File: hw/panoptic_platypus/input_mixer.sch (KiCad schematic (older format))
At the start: 9 parts

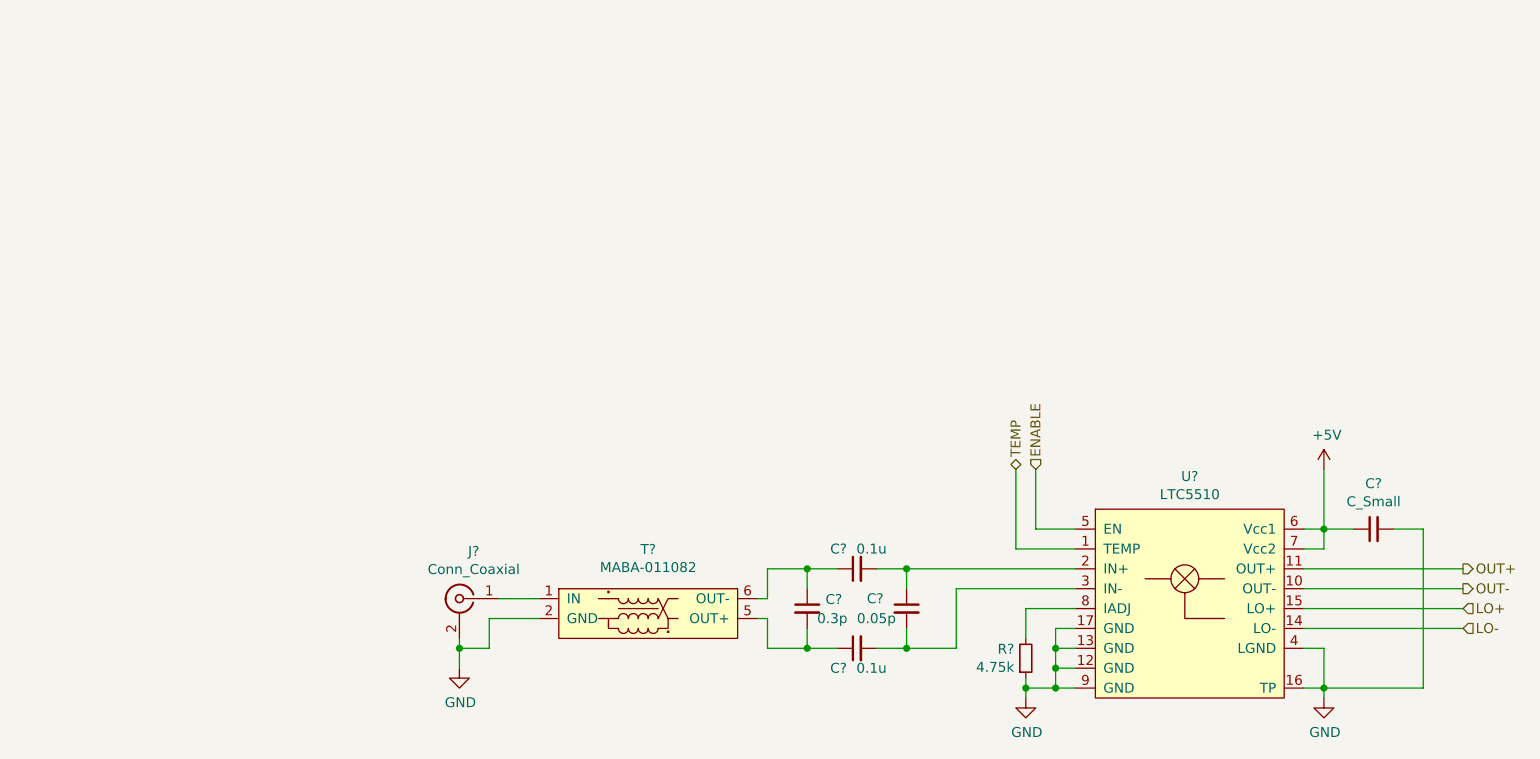
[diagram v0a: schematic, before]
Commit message: Added ADC decoupling and input filter
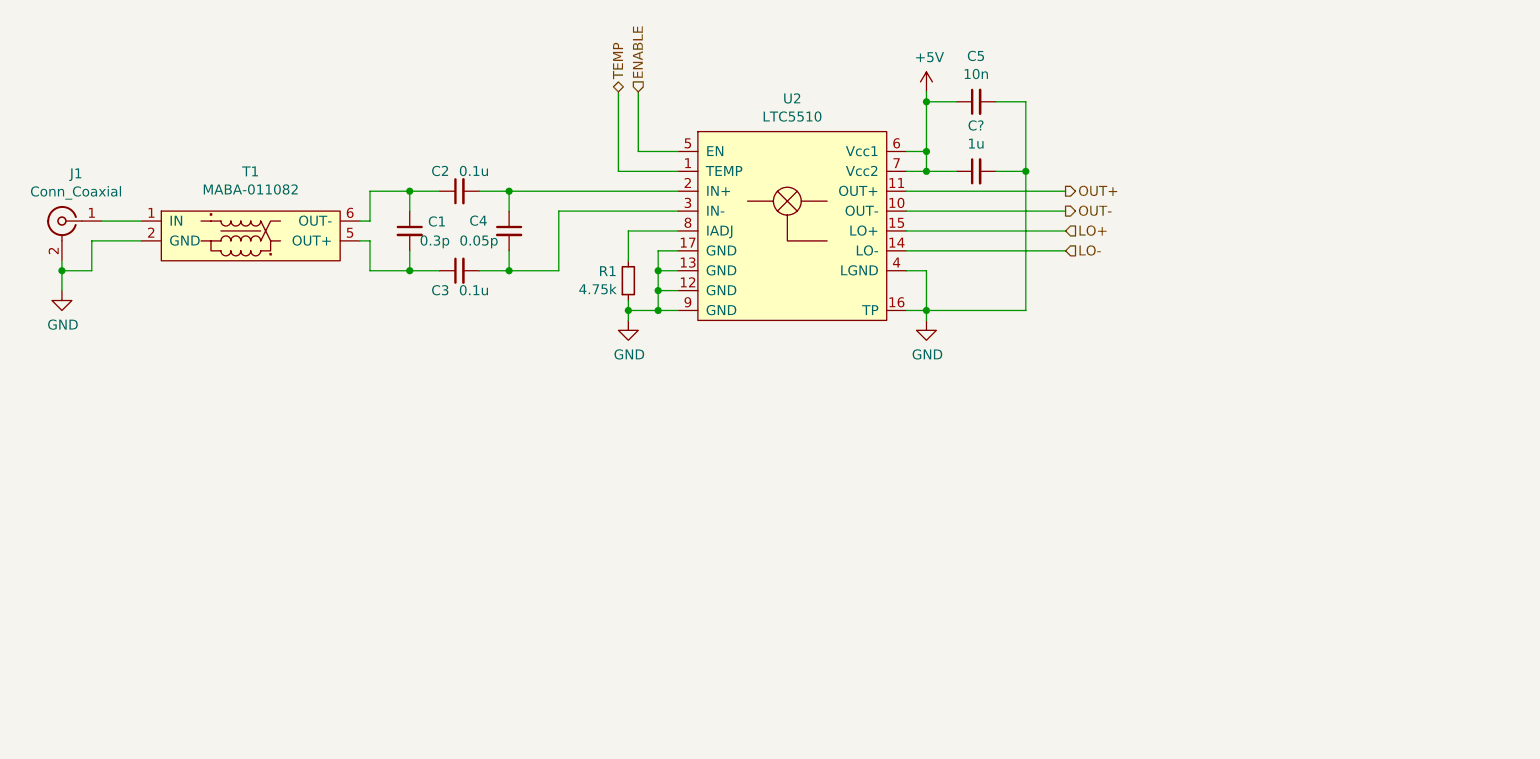
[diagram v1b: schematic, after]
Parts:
- added C?: 1u, symbol Device:C_Small
- C5: renamed from C?; value C_Small -> 10n
- gave numbers to parts that had none: 8
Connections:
- net +5V: now also C?.1
- net GND: now also C?.2
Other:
- moved on the sheet: C1, C2, C3, C4, C5, J1, R1, T1, U2

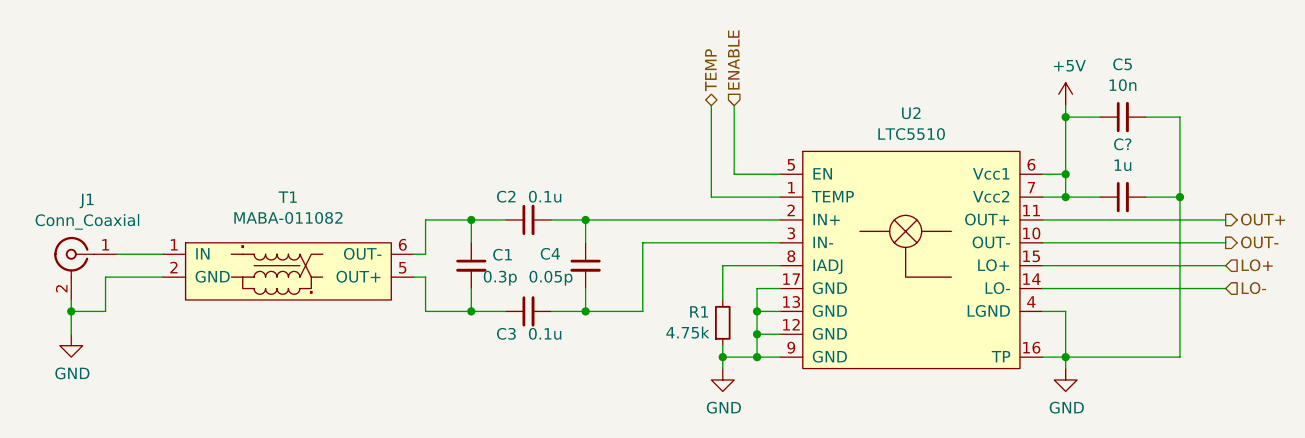
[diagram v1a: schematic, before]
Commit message: updated some symbols added some ICs
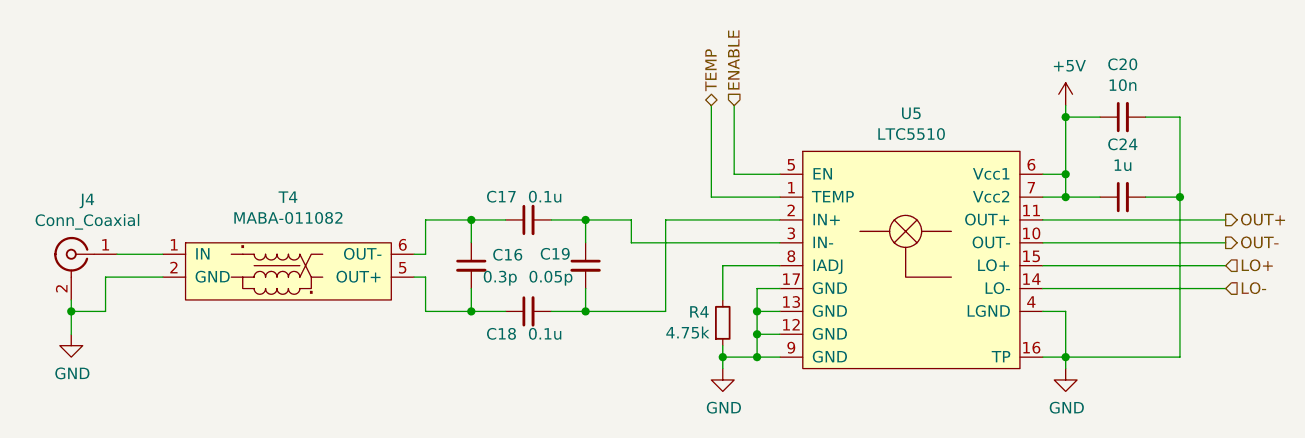
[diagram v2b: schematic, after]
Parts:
- C1, C2, C3, C4, C5: footprint (none) -> Capacitor_SMD:C_0402_1005Metric
- C21: renamed from C?; footprint (none) -> Capacitor_SMD:C_0402_1005Metric
- J1: footprint (none) -> Connector_Coaxial:SMA_Amphenol_132289_EdgeMount
- R1: footprint (none) -> Resistor_SMD:R_0402_1005Metric
- T1: footprint (none) -> Transformer_SMD:Pulse_P0926NL
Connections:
- net at C2.2, C4.1: now also U2.3 (IN-); no longer U2.2 (IN+)
- net at C3.2, C4.2: now also U2.2 (IN+); no longer U2.3 (IN-)
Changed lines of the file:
@@
 $Descr A4 11693 8268
 encoding utf-8
-Sheet 2 6
+Sheet 5 9
 Title ""
 Date "2020-09-21"
@@
 AR Path="/5F682454/5F68ECDE" Ref="J3"  Part="1"
 AR Path="/5F682640/5F68ECDE" Ref="J4"  Part="1"
-F 0 "J1" H 1128 2338 50  0000 C CNN
+F 0 "J4" H 1128 2338 50  0000 C CNN
 F 1 "Conn_Coaxial" H 1128 2247 50  0000 C CNN
-F 2 "" H 1200 2100 50  0001 C CNN
+F 2 "Connector_Coaxial:SMA_Amphenol_132289_EdgeMount" H 1200 2100 50  0001 C CNN
 F 3 " ~" H 1200 2100 50  0001 C CNN
 	1    1200 2100
@@
 AR Path="/5F682454/5F68ECE4" Ref="U4"  Part="1"
 AR Path="/5F682640/5F68ECE4" Ref="U5"  Part="1"
-F 0 "U2" H 4875 2315 50  0000 C CNN
+F 0 "U5" H 4875 2315 50  0000 C CNN
 F 1 "LTC5510" H 4875 2224 50  0000 C CNN
 F 2 "Package_DFN_QFN:QFN-16-1EP_5x5mm_P0.8mm_EP2.7x2.7mm_ThermalVias" H 5200 2450 50  0001 C CNN
@@
 AR Path="/5F682454/5F68ECEA" Ref="T3"  Part="1"
 AR Path="/5F682640/5F68ECEA" Ref="T4"  Part="1"
-F 0 "T1" H 2150 2448 50  0000 C CNN
+F 0 "T4" H 2150 2448 50  0000 C CNN
 F 1 "MABA-011082" H 2150 2357 50  0000 C CNN
-F 2 "" H 2100 2600 50  0001 C CNN
+F 2 "Transformer_SMD:Pulse_P0926NL" H 2100 2600 50  0001 C CNN
 F 3 "https://cdn.macom.com/datasheets/MABA-011082.pdf" H 2100 2600 50  0001 C CNN
 	1    2100 2150
@@
 AR Path="/5F682454/5F68ECF1" Ref="C11"  Part="1"
 AR Path="/5F682640/5F68ECF1" Ref="C16"  Part="1"
-F 0 "C1" H 3042 2196 50  0000 L CNN
+F 0 "C16" H 3042 2196 50  0000 L CNN
 F 1 "0.3p" H 3000 2100 50  0000 L CNN
-F 2 "" H 2950 2150 50  0001 C CNN
+F 2 "Capacitor_SMD:C_0402_1005Metric" H 2950 2150 50  0001 C CNN
 F 3 "~" H 2950 2150 50  0001 C CNN
 	1    2950 2150
@@
 AR Path="/5F682454/5F68ECF7" Ref="C12"  Part="1"
 AR Path="/5F682640/5F68ECF7" Ref="C17"  Part="1"
-F 0 "C2" V 3300 2000 50  0000 L CNN
+F 0 "C17" V 3300 2000 50  0000 L CNN
 F 1 "0.1u" V 3300 1800 50  0000 L CNN
-F 2 "" H 3200 1950 50  0001 C CNN
+F 2 "Capacitor_SMD:C_0402_1005Metric" H 3200 1950 50  0001 C CNN
 F 3 "~" H 3200 1950 50  0001 C CNN
 	1    3200 1950
@@
 AR Path="/5F682454/5F68ECFD" Ref="C13"  Part="1"
 AR Path="/5F682640/5F68ECFD" Ref="C18"  Part="1"
-F 0 "C3" V 3300 2400 50  0000 L CNN
+F 0 "C18" V 3300 2400 50  0000 L CNN
 F 1 "0.1u" V 3300 2200 50  0000 L CNN
-F 2 "" H 3200 2350 50  0001 C CNN
+F 2 "Capacitor_SMD:C_0402_1005Metric" H 3200 2350 50  0001 C CNN
 F 3 "~" H 3200 2350 50  0001 C CNN
 	1    3200 2350
@@
 AR Path="/5F682454/5F68ED03" Ref="C14"  Part="1"
 AR Path="/5F682640/5F68ED03" Ref="C19"  Part="1"
-F 0 "C4" H 3250 2200 50  0000 L CNN
+F 0 "C19" H 3250 2200 50  0000 L CNN
 F 1 "0.05p" H 3200 2100 50  0000 L CNN
-F 2 "" H 3450 2150 50  0001 C CNN
+F 2 "Capacitor_SMD:C_0402_1005Metric" H 3450 2150 50  0001 C CNN
 F 3 "~" H 3450 2150 50  0001 C CNN
 	1    3450 2150
@@
 Wire Wire Line
 	2950 2350 3100 2350
-Connection ~ 3450 1950
-Connection ~ 3450 2350
 $Comp
 L power:GND #PWR?
@@
 AR Path="/5F682454/5F68ED1F" Ref="#PWR0109"  Part="1"
 AR Path="/5F682640/5F68ED1F" Ref="#PWR0113"  Part="1"
-F 0 "#PWR0101" H 1200 2200 50  0001 C CNN
+F 0 "#PWR0113" H 1200 2200 50  0001 C CNN
 F 1 "GND" H 1205 2277 50  0000 C CNN
 F 2 "" H 1200 2450 50  0001 C CNN
@@
 AR Path="/5F682454/5F68ED27" Ref="R3"  Part="1"
 AR Path="/5F682640/5F68ED27" Ref="R4"  Part="1"
-F 0 "R1" H 3992 2354 50  0000 R CNN
+F 0 "R4" H 3992 2354 50  0000 R CNN
 F 1 "4.75k" H 3992 2445 50  0000 R CNN
-F 2 "" H 4050 2400 50  0001 C CNN
+F 2 "Resistor_SMD:R_0402_1005Metric" H 4050 2400 50  0001 C CNN
 F 3 "~" H 4050 2400 50  0001 C CNN
 	1    4050 2400
@@
 AR Path="/5F682454/5F68ED3D" Ref="#PWR0110"  Part="1"
 AR Path="/5F682640/5F68ED3D" Ref="#PWR0114"  Part="1"
-F 0 "#PWR0102" H 4050 2350 50  0001 C CNN
+F 0 "#PWR0114" H 4050 2350 50  0001 C CNN
 F 1 "GND" H 4055 2427 50  0000 C CNN
 F 2 "" H 4050 2600 50  0001 C CNN
@@
 AR Path="/5F682454/5F690C99" Ref="#PWR0111"  Part="1"
 AR Path="/5F682640/5F690C99" Ref="#PWR0115"  Part="1"
-F 0 "#PWR0103" H 5550 2350 50  0001 C CNN
+F 0 "#PWR0115" H 5550 2350 50  0001 C CNN
 F 1 "GND" H 5555 2427 50  0000 C CNN
 F 2 "" H 5550 2600 50  0001 C CNN
@@
 AR Path="/5F682454/5F6919E0" Ref="#PWR0112"  Part="1"
 AR Path="/5F682640/5F6919E0" Ref="#PWR0116"  Part="1"
-F 0 "#PWR0104" H 5550 1300 50  0001 C CNN
+F 0 "#PWR0116" H 5550 1300 50  0001 C CNN
 F 1 "+5V" H 5565 1623 50  0000 C CNN
 F 2 "" H 5550 1450 50  0001 C CNN
@@
 Wire Wire Line
 	5550 1750 5550 1850
-Wire Wire Line
-	3700 2350 3700 2050
-Wire Wire Line
-	3450 2350 3700 2350
-Wire Wire Line
-	3450 1950 4300 1950
-Wire Wire Line
-	3700 2050 4300 2050
 Wire Wire Line
 	4300 1750 4100 1750
@@
 AR Path="/5F682454/5F6B3658" Ref="C15"  Part="1"
 AR Path="/5F682640/5F6B3658" Ref="C20"  Part="1"
-F 0 "C5" V 6029 1500 50  0000 C CNN
+F 0 "C20" V 6029 1500 50  0000 C CNN
 F 1 "10n" V 5938 1500 50  0000 C CNN
-F 2 "" H 5800 1500 50  0001 C CNN
+F 2 "Capacitor_SMD:C_0402_1005Metric" H 5800 1500 50  0001 C CNN
 F 3 "~" H 5800 1500 50  0001 C CNN
 	1    5800 1500
@@
 AR Path="/5F72B3DB/5F71DE7D" Ref="C?"  Part="1"
 AR Path="/5F72B5D5/5F71DE7D" Ref="C?"  Part="1"
-AR Path="/5F68A5E9/5F71DE7D" Ref="C?"  Part="1"
+AR Path="/5F68A5E9/5F71DE7D" Ref="C21"  Part="1"
 AR Path="/5F69642F/5F71DE7D" Ref="C?"  Part="1"
 AR Path="/5F696622/5F71DE7D" Ref="C?"  Part="1"
 AR Path="/5F69684D/5F71DE7D" Ref="C?"  Part="1"
-AR Path="/5F68220D/5F71DE7D" Ref="C?"  Part="1"
-AR Path="/5F682454/5F71DE7D" Ref="C?"  Part="1"
-AR Path="/5F682640/5F71DE7D" Ref="C?"  Part="1"
-F 0 "C?" V 6029 1850 50  0000 C CNN
+AR Path="/5F68220D/5F71DE7D" Ref="C22"  Part="1"
+AR Path="/5F682454/5F71DE7D" Ref="C23"  Part="1"
+AR Path="/5F682640/5F71DE7D" Ref="C24"  Part="1"
+F 0 "C24" V 6029 1850 50  0000 C CNN
 F 1 "1u" V 5938 1850 50  0000 C CNN
-F 2 "" H 5800 1850 50  0001 C CNN
+F 2 "Capacitor_SMD:C_0402_1005Metric" H 5800 1850 50  0001 C CNN
 F 3 "~" H 5800 1850 50  0001 C CNN
 	1    5800 1850
@@
 Wire Wire Line
 	5550 1500 5550 1750
+Connection ~ 3450 2350
+Wire Wire Line
+	3800 2350 3800 1950
+Wire Wire Line
+	3800 1950 4300 1950
+Wire Wire Line
+	3450 2350 3800 2350
+Wire Wire Line
+	3450 1950 3650 1950
+Wire Wire Line
+	3650 1950 3650 2050
+Wire Wire Line
+	3650 2050 4300 2050
+Connection ~ 3450 1950
 $EndSCHEMATC

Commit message: Added LO Generator, fixed some smybols
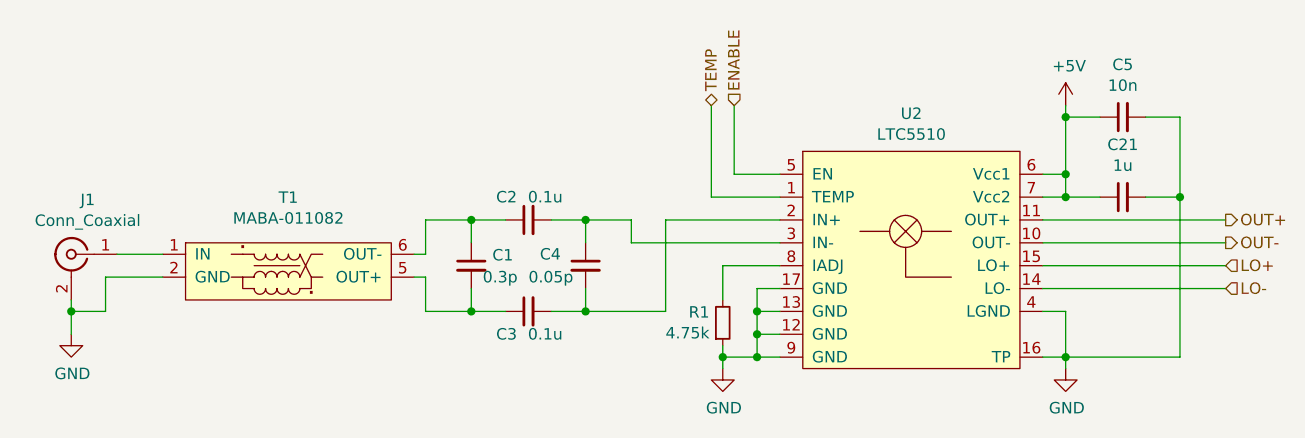
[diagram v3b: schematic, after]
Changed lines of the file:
@@
 $Descr A4 11693 8268
 encoding utf-8
-Sheet 5 9
+Sheet 2 12
 Title ""
 Date "2020-09-21"
@@
 AR Path="/5F682454/5F68ECDE" Ref="J3"  Part="1"
 AR Path="/5F682640/5F68ECDE" Ref="J4"  Part="1"
-F 0 "J4" H 1128 2338 50  0000 C CNN
+F 0 "J1" H 1128 2338 50  0000 C CNN
 F 1 "Conn_Coaxial" H 1128 2247 50  0000 C CNN
 F 2 "Connector_Coaxial:SMA_Amphenol_132289_EdgeMount" H 1200 2100 50  0001 C CNN
@@
 AR Path="/5F682454/5F68ECE4" Ref="U4"  Part="1"
 AR Path="/5F682640/5F68ECE4" Ref="U5"  Part="1"
-F 0 "U5" H 4875 2315 50  0000 C CNN
+F 0 "U2" H 4875 2315 50  0000 C CNN
 F 1 "LTC5510" H 4875 2224 50  0000 C CNN
 F 2 "Package_DFN_QFN:QFN-16-1EP_5x5mm_P0.8mm_EP2.7x2.7mm_ThermalVias" H 5200 2450 50  0001 C CNN
@@
 AR Path="/5F682454/5F68ECEA" Ref="T3"  Part="1"
 AR Path="/5F682640/5F68ECEA" Ref="T4"  Part="1"
-F 0 "T4" H 2150 2448 50  0000 C CNN
+F 0 "T1" H 2150 2448 50  0000 C CNN
 F 1 "MABA-011082" H 2150 2357 50  0000 C CNN
 F 2 "Transformer_SMD:Pulse_P0926NL" H 2100 2600 50  0001 C CNN
@@
 AR Path="/5F682454/5F68ECF1" Ref="C11"  Part="1"
 AR Path="/5F682640/5F68ECF1" Ref="C16"  Part="1"
-F 0 "C16" H 3042 2196 50  0000 L CNN
+F 0 "C1" H 3042 2196 50  0000 L CNN
 F 1 "0.3p" H 3000 2100 50  0000 L CNN
 F 2 "Capacitor_SMD:C_0402_1005Metric" H 2950 2150 50  0001 C CNN
@@
 AR Path="/5F682454/5F68ECF7" Ref="C12"  Part="1"
 AR Path="/5F682640/5F68ECF7" Ref="C17"  Part="1"
-F 0 "C17" V 3300 2000 50  0000 L CNN
+F 0 "C2" V 3300 2000 50  0000 L CNN
 F 1 "0.1u" V 3300 1800 50  0000 L CNN
 F 2 "Capacitor_SMD:C_0402_1005Metric" H 3200 1950 50  0001 C CNN
@@
 AR Path="/5F682454/5F68ECFD" Ref="C13"  Part="1"
 AR Path="/5F682640/5F68ECFD" Ref="C18"  Part="1"
-F 0 "C18" V 3300 2400 50  0000 L CNN
+F 0 "C3" V 3300 2400 50  0000 L CNN
 F 1 "0.1u" V 3300 2200 50  0000 L CNN
 F 2 "Capacitor_SMD:C_0402_1005Metric" H 3200 2350 50  0001 C CNN
@@
 AR Path="/5F682454/5F68ED03" Ref="C14"  Part="1"
 AR Path="/5F682640/5F68ED03" Ref="C19"  Part="1"
-F 0 "C19" H 3250 2200 50  0000 L CNN
+F 0 "C4" H 3250 2200 50  0000 L CNN
 F 1 "0.05p" H 3200 2100 50  0000 L CNN
 F 2 "Capacitor_SMD:C_0402_1005Metric" H 3450 2150 50  0001 C CNN
@@
 AR Path="/5F682454/5F68ED27" Ref="R3"  Part="1"
 AR Path="/5F682640/5F68ED27" Ref="R4"  Part="1"
-F 0 "R4" H 3992 2354 50  0000 R CNN
+F 0 "R1" H 3992 2354 50  0000 R CNN
 F 1 "4.75k" H 3992 2445 50  0000 R CNN
 F 2 "Resistor_SMD:R_0402_1005Metric" H 4050 2400 50  0001 C CNN
@@
 AR Path="/5F682454/5F6B3658" Ref="C15"  Part="1"
 AR Path="/5F682640/5F6B3658" Ref="C20"  Part="1"
-F 0 "C20" V 6029 1500 50  0000 C CNN
+F 0 "C5" V 6029 1500 50  0000 C CNN
 F 1 "10n" V 5938 1500 50  0000 C CNN
 F 2 "Capacitor_SMD:C_0402_1005Metric" H 5800 1500 50  0001 C CNN
@@
 AR Path="/5F682454/5F71DE7D" Ref="C23"  Part="1"
 AR Path="/5F682640/5F71DE7D" Ref="C24"  Part="1"
-F 0 "C24" V 6029 1850 50  0000 C CNN
+F 0 "C21" V 6029 1850 50  0000 C CNN
 F 1 "1u" V 5938 1850 50  0000 C CNN
 F 2 "Capacitor_SMD:C_0402_1005Metric" H 5800 1850 50  0001 C CNN
